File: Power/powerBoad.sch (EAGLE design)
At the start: 22 parts, among them CON1 MR30PW-M, CON2 XT30PW-M, U1 V7805-1000, U2 LD1117S33CTR, X1 JST-XH-06-PIN-LONG-PAD, X2 JST-XH-06-PIN-LONG-PAD, X3 JST-XH-06-PIN-LONG-PAD, X4 JST-XH-06-PIN-LONG-PAD

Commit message: 回路図と部品配置を検討し始めた
これからも検討に検討を重ね検討したいと思う。
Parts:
- removed U$7: XT30UPB-M, XT30UPB-M:XT30UPB-M
- added CON3: XT30PW-M, amass:XT30PW-M
- added J1: (no value), SparkFun-Connectors:CONN_05JST
- added KICK: (no value), jst-xh:S4B-XH-A
- added MC1, MC33151: MC33151DR2G, MC33151DR2G:MC33151DR2G
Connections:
- new net KICK1: MC33151.LOGIC_I/P_A
- new net KICK2: MC1.LOGIC_I/P_A
- new net KICK_V: KICK.2, MC33151.DRIVE_O/P_A
- new net KICK_V2: KICK.3, MC1.DRIVE_O/P_A
- new net TR_IN: KICK.4
- net +15V: now also CON3.+, MC1.VCC, MC33151.VCC; no longer U$7.1
- net +5V: now also KICK.1
- net GND: now also CON3.-, MC1.GND, MC33151.GND; no longer U$7.2
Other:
- note added: "Kick"
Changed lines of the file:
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@@
 <part name="+3V1" library="supply1" library_urn="urn:adsk.eagle:library:371" deviceset="+3V3" device=""/>
 <part name="P+5" library="supply1" library_urn="urn:adsk.eagle:library:371" deviceset="+15V" device=""/>
-<part name="U$7" library="XT30UPB-M" deviceset="XT30UPB-M" device=""/>
 <part name="D1" library="SS14" deviceset="SS14" device=""/>
 <part name="C1" library="rcl" library_urn="urn:adsk.eagle:library:334" deviceset="C-EU" device="C1608" package3d_urn="urn:adsk.eagle:package:23621/2" value="0.1u"/>
@@
 <part name="X3" library="Rembrandt Electronics - JST XH Connectors v1-0" deviceset="JST-XH-06-PIN" device="-LONG-PAD"/>
 <part name="X4" library="Rembrandt Electronics - JST XH Connectors v1-0" deviceset="JST-XH-06-PIN" device="-LONG-PAD"/>
+<part name="MC33151" library="MC33151DR2G" deviceset="MC33151DR2G" device=""/>
+<part name="P+3" library="supply1" library_urn="urn:adsk.eagle:library:371" deviceset="+15V" device=""/>
+<part name="MC1" library="MC33151DR2G" deviceset="MC33151DR2G" device=""/>
+<part name="GND2" library="supply1" library_urn="urn:adsk.eagle:library:371" deviceset="GND" device=""/>
+<part name="P+10" library="supply1" library_urn="urn:adsk.eagle:library:371" deviceset="+5V" device=""/>
+<part name="KICK" library="jst-xh" deviceset="S4B-XH-A" device=""/>
+<part name="CON3" library="amass" deviceset="XT30" device="PW-M"/>
+<part name="J1" library="SparkFun-Connectors" library_urn="urn:adsk.eagle:library:513" deviceset="CONN_05" device="JST" package3d_urn="urn:adsk.eagle:package:38120/1"/>
 </parts>
 <sheets>
@@
 <text x="-38.1" y="17.78" size="3.81" layer="94">Power</text>
 <text x="43.18" y="-38.1" size="3.81" layer="94">Dribbler</text>
+<text x="83.82" y="12.7" size="3.81" layer="94">Kick</text>
 </plain>
 <instances>
@@
 <attribute name="VALUE" x="58.42" y="-50.8" size="1.778" layer="96" rot="R90"/>
 </instance>
-<instance part="U$7" gate="G$1" x="-22.86" y="-38.1" smashed="yes"/>
 <instance part="D1" gate="G$1" x="-12.7" y="-71.12" smashed="yes" rot="R90">
 <attribute name="NAME" x="-15.24" y="-76.2" size="1.778" layer="95" rot="R90"/>
@@
 <instance part="X4" gate="-6" x="121.285" y="-82.55" smashed="yes">
 <attribute name="NAME" x="123.825" y="-83.312" size="1.524" layer="95"/>
+</instance>
+<instance part="MC33151" gate="G$1" x="91.44" y="2.54" smashed="yes">
+<attribute name="VALUE" x="90.17" y="7.62" size="1.778" layer="96" align="center-left"/>
+</instance>
+<instance part="P+3" gate="1" x="139.7" y="15.24" smashed="yes">
+<attribute name="VALUE" x="137.16" y="10.16" size="1.778" layer="96" rot="R90"/>
+</instance>
+<instance part="MC1" gate="G$1" x="91.44" y="-15.24" smashed="yes">
+<attribute name="VALUE" x="90.17" y="-10.16" size="1.778" layer="96" align="center-left"/>
+</instance>
+<instance part="GND2" gate="1" x="88.9" y="-33.02" smashed="yes">
+<attribute name="VALUE" x="86.36" y="-35.56" size="1.778" layer="96"/>
+</instance>
+<instance part="P+10" gate="1" x="88.9" y="38.1" smashed="yes">
+<attribute name="VALUE" x="86.36" y="33.02" size="1.778" layer="96" rot="R90"/>
+</instance>
+<instance part="KICK" gate="G$1" x="106.68" y="27.94" smashed="yes">
+<attribute name="NAME" x="102.87" y="34.29" size="1.778" layer="95"/>
+<attribute name="VALUE" x="102.87" y="17.78" size="1.778" layer="96"/>
+</instance>
+<instance part="CON3" gate="G$1" x="33.02" y="-40.64" smashed="yes">
+<attribute name="VALUE" x="29.21" y="-49.53" size="1.778" layer="96"/>
+<attribute name="NAME" x="29.21" y="-33.528" size="1.778" layer="95"/>
+</instance>
+<instance part="J1" gate="G$1" x="43.18" y="17.78" smashed="yes">
+<attribute name="VALUE" x="40.64" y="7.874" size="1.778" layer="96" font="vector"/>
+<attribute name="NAME" x="40.64" y="25.908" size="1.778" layer="95" font="vector"/>
 </instance>
 </instances>
@@
 <wire x1="-33.02" y1="-40.64" x2="-33.02" y2="-50.8" width="0.1524" layer="91"/>
 <pinref part="GND16" gate="1" pin="GND"/>
-<wire x1="-15.24" y1="-40.64" x2="-27.94" y2="-40.64" width="0.1524" layer="91"/>
+<wire x1="-15.24" y1="-40.64" x2="-33.02" y2="-40.64" width="0.1524" layer="91"/>
 <pinref part="U$2" gate="G$1" pin="2"/>
-<wire x1="-27.94" y1="-40.64" x2="-33.02" y2="-40.64" width="0.1524" layer="91"/>
-<pinref part="U$7" gate="G$1" pin="2"/>
-<junction x="-27.94" y="-40.64"/>
 <pinref part="CON2" gate="G$1" pin="-"/>
 <wire x1="22.86" y1="-43.18" x2="22.86" y2="-40.64" width="0.1524" layer="91"/>
 <wire x1="22.86" y1="-40.64" x2="-15.24" y2="-40.64" width="0.1524" layer="91"/>
 <junction x="-15.24" y="-40.64"/>
+<pinref part="CON3" gate="G$1" pin="-"/>
+<wire x1="38.1" y1="-43.18" x2="38.1" y2="-40.64" width="0.1524" layer="91"/>
+<wire x1="38.1" y1="-40.64" x2="22.86" y2="-40.64" width="0.1524" layer="91"/>
+<junction x="22.86" y="-40.64"/>
 </segment>
 <segment>
@@
 <pinref part="X4" gate="-3" pin="S"/>
 </segment>
+<segment>
+<pinref part="GND2" gate="1" pin="GND"/>
+<wire x1="88.9" y1="-20.32" x2="88.9" y2="-30.48" width="0.1524" layer="91"/>
+<pinref part="MC1" gate="G$1" pin="GND"/>
+<wire x1="91.44" y1="-20.32" x2="88.9" y2="-20.32" width="0.1524" layer="91"/>
+<pinref part="MC33151" gate="G$1" pin="GND"/>
+<wire x1="91.44" y1="-2.54" x2="88.9" y2="-2.54" width="0.1524" layer="91"/>
+<wire x1="88.9" y1="-2.54" x2="88.9" y2="-20.32" width="0.1524" layer="91"/>
+<junction x="88.9" y="-20.32"/>
+</segment>
 </net>
 <net name="+5V" class="0">
@@
 <junction x="12.7" y="-2.54"/>
 </segment>
+<segment>
+<wire x1="88.9" y1="30.48" x2="106.68" y2="30.48" width="0.1524" layer="91"/>
+<pinref part="P+10" gate="1" pin="+5V"/>
+<wire x1="88.9" y1="30.48" x2="88.9" y2="35.56" width="0.1524" layer="91"/>
+<pinref part="KICK" gate="G$1" pin="1"/>
+</segment>
 </net>
 <net name="+3V3" class="0">
@@
 <segment>
 <wire x1="-33.02" y1="-38.1" x2="-33.02" y2="-30.48" width="0.1524" layer="91"/>
-<wire x1="-15.24" y1="-38.1" x2="-27.94" y2="-38.1" width="0.1524" layer="91"/>
+<wire x1="-15.24" y1="-38.1" x2="-33.02" y2="-38.1" width="0.1524" layer="91"/>
 <pinref part="P+13" gate="1" pin="+15V"/>
 <pinref part="U$2" gate="G$1" pin="1"/>
-<wire x1="-27.94" y1="-38.1" x2="-33.02" y2="-38.1" width="0.1524" layer="91"/>
 <junction x="-15.24" y="-38.1"/>
-<pinref part="U$7" gate="G$1" pin="1"/>
-<junction x="-27.94" y="-38.1"/>
 <pinref part="CON2" gate="G$1" pin="+"/>
 <wire x1="-15.24" y1="-38.1" x2="22.86" y2="-38.1" width="0.1524" layer="91"/>
+<pinref part="CON3" gate="G$1" pin="+"/>
+<wire x1="38.1" y1="-38.1" x2="22.86" y2="-38.1" width="0.1524" layer="91"/>
+<junction x="22.86" y="-38.1"/>
 </segment>
 <segment>
@@
 <pinref part="CON1" gate="G$1" pin="2"/>
 <wire x1="55.88" y1="-63.5" x2="60.96" y2="-63.5" width="0.1524" layer="91"/>
+</segment>
+<segment>
+<pinref part="MC33151" gate="G$1" pin="VCC"/>
+<wire x1="137.16" y1="-2.54" x2="139.7" y2="-2.54" width="0.1524" layer="91"/>
+<wire x1="139.7" y1="-2.54" x2="139.7" y2="12.7" width="0.1524" layer="91"/>
+<pinref part="P+3" gate="1" pin="+15V"/>
+<pinref part="MC1" gate="G$1" pin="VCC"/>
+<wire x1="137.16" y1="-20.32" x2="139.7" y2="-20.32" width="0.1524" layer="91"/>
+<wire x1="139.7" y1="-20.32" x2="139.7" y2="-2.54" width="0.1524" layer="91"/>
+<junction x="139.7" y="-2.54"/>
 </segment>
 </net>
@@
 </segment>
 </net>
+<net name="KICK2" class="0">
+<segment>
+<pinref part="MC1" gate="G$1" pin="LOGIC_I/P_A"/>
+<wire x1="91.44" y1="-17.78" x2="86.36" y2="-17.78" width="0.1524" layer="91"/>
+<label x="86.36" y="-17.78" size="0.762" layer="95" rot="R180" xref="yes"/>
+</segment>
+</net>
+<net name="KICK_V2" class="0">
+<segment>
+<pinref part="MC1" gate="G$1" pin="DRIVE_O/P_A"/>
+<wire x1="137.16" y1="-17.78" x2="142.24" y2="-17.78" width="0.1524" layer="91"/>
+<label x="142.24" y="-17.78" size="0.762" layer="95" xref="yes"/>
+</segment>
+<segment>
+<wire x1="106.68" y1="25.4" x2="91.44" y2="25.4" width="0.1524" layer="91"/>
+<pinref part="KICK" gate="G$1" pin="3"/>
+<label x="91.44" y="25.4" size="0.762" layer="95" rot="R180" xref="yes"/>
+</segment>
+</net>
+<net name="KICK_V" class="0">
+<segment>
+<pinref part="MC33151" gate="G$1" pin="DRIVE_O/P_A"/>
+<wire x1="137.16" y1="0" x2="142.24" y2="0" width="0.1524" layer="91"/>
+<label x="142.24" y="0" size="0.762" layer="95" xref="yes"/>
+</segment>
+<segment>
+<wire x1="106.68" y1="27.94" x2="91.44" y2="27.94" width="0.1524" layer="91"/>
+<pinref part="KICK" gate="G$1" pin="2"/>
+<label x="91.44" y="27.94" size="0.762" layer="95" rot="R180" xref="yes"/>
+</segment>
+</net>
+<net name="KICK1" class="0">
+<segment>
+<pinref part="MC33151" gate="G$1" pin="LOGIC_I/P_A"/>
+<wire x1="91.44" y1="0" x2="86.36" y2="0" width="0.1524" layer="91"/>
+<label x="86.36" y="0" size="0.762" layer="95" rot="R180" xref="yes"/>
+</segment>
+</net>
+<net name="TR_IN" class="0">
+<segment>
+<wire x1="106.68" y1="22.86" x2="91.44" y2="22.86" width="0.1524" layer="91"/>
+<pinref part="KICK" gate="G$1" pin="4"/>
+<label x="91.44" y="22.86" size="0.762" layer="95" rot="R180" xref="yes"/>
+</segment>
+</net>

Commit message: some update 部品配置
# ==== Emojis ====
# ✨ :sparkles: Add new feature
# ✅  :white_check_mark: Update existing feature (not bug)
# ⚠️  :warning: Fix bug/error
# 🔥  :fire: Remove files or features
# ✏️ :pencil2: Fix typos
# 📝  :memo: Update documentation
# ♻️  :recycle: Dependencies update
# 🐧  :penguin: Improved the Linux
# 🍎  :apple: Improved the macOS
# 🔖 :bookmark: Add new library
# 🎉  :tada: Initial commit

# ==== Format ====
# :emoji: Subject
#
# Commit body...

# ==== Messages ====
# 新規(ファイル)機能追加: Add
# 機能修正、既存機能追加（バグではない): Update
# リファクタリング: Clean
# ファイル名変更:
# 削除など: Remove
# バグ修正: Fix
# バージョンアップ: Upgrade
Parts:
- removed J1: (no value), SparkFun-Connectors:CONN_05JST
- removed U$2: XT30UPB-M, XT30UPB-M:XT30UPB-M
- removed X1, X2, X3, X4: JST-XH-06-PIN-LONG-PAD, Rembrandt Electronics - JST XH Connectors v1-0:JST-XH-06-PIN-LONG-PAD
- added CN1, CN2, CN3, CN4: (no value), jst-xh:S6B-XH-A
- added JP1, JP2: (no value), adafruit:PINHD-1X6
- renumbered MC1 to U4, MC33151 to U3
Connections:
- removed net DR_PWM: CON1.1
- removed net TR_IN: KICK.4
- removed net VOLT_SIG: D1.K
- new net BAT: D1.K, JP1.1
- new net DRIB_PWM: CON1.1, JP1.4
- new net GPIO0: JP1.6
- new net PHOTO: JP1.5, KICK.4
- net +15V: now also JP2.1; no longer U$2.1
- net +3V3: now also JP2.3
- net +5V: now also JP2.2
- net 5V: now also CN1.3, CN2.3, CN3.3, CN4.3; no longer X1-4.S, X2-4.S, X3-4.S, X4-4.S
- net CANH: now also CN1.2, CN2.2, CN3.2, CN4.2, JP1.2; no longer X1-5.S, X2-5.S, X3-5.S, X4-5.S
- net CANL: now also CN1.1, CN2.1, CN3.1, CN4.1, JP1.3; no longer X1-6.S, X2-6.S, X3-6.S, X4-6.S
- net GND: now also CN1.4, CN2.4, CN3.4, CN4.4, JP2.4; no longer U$2.2, X1-3.S, X2-3.S, X3-3.S, X4-3.S
- net GVDD_IN: now also CN1.6, CN2.6, CN3.6, CN4.6; no longer X1-1.S, X2-1.S, X3-1.S, X4-1.S
- net KICK1: now also JP2.5
- net KICK2: now also JP2.6
- net PVDD: now also CN1.5, CN2.5, CN3.5, CN4.5; no longer X1-2.S, X2-2.S, X3-2.S, X4-2.S
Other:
- note added: "battery"

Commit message: POWERをいい感じにした
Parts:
- removed R5: 100k, rcl:R-EU_0207/10
- removed R6: 470k, rcl:R-EU_0207/10
- added LED3: (no value), led:LEDCHIPLED_0603
- added R2: 470k, rcl:R-EU_R0603
- added R3: 100k, rcl:R-EU_R0603
- added R4: 5k, rcl:R-EU_R0603
- LED1: device led:LEDCHIP-LED0805 -> led:LEDCHIPLED_0603
- R1: value (none) -> 1k
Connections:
- net GVDD_IN renamed GVDD
- removed net +15V: C3.1, C8.+, CON1.2, CON2.+, CON3.+, JP2.1, R6.1, U1.+VIN, U3.VCC, U4.VCC
- removed net 5V: CN1.3, CN2.3, CN3.3, CN4.3
- removed net LED: R1.2
- new net N$1: LED3.A, R4.1
- net +3V3: now also R1.2
- net +5V: now also CN1.3, CN2.3, CN3.3, CN4.3, R4.2
- net 2: now also R2.2, R3.2; no longer R5.2, R6.2
- net GND: now also LED3.C, R3.1; no longer R5.1
- net PVDD: now also C3.1, C8.+, CON1.2, CON2.+, CON3.+, JP2.1, R2.1, U1.+VIN, U3.VCC, U4.VCC
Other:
- moved on the sheet: LED1

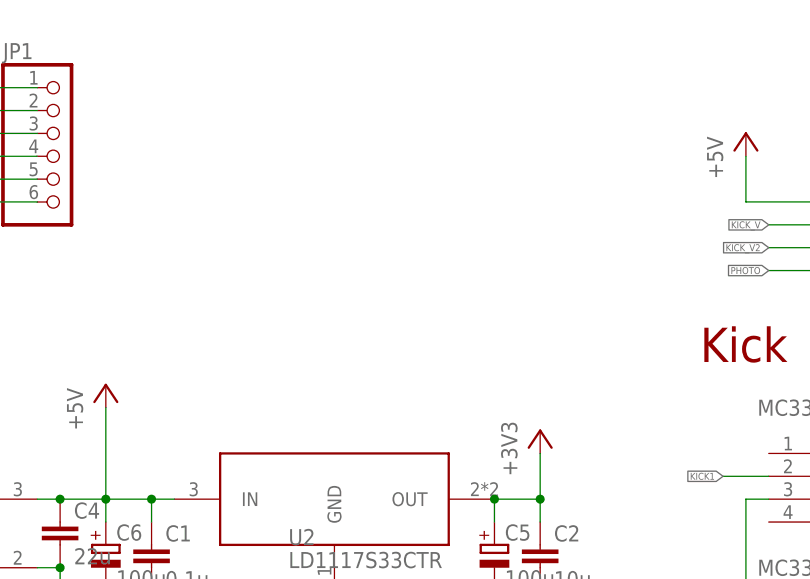
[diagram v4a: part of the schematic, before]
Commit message: 可変レギュレータを追加して配線をやりきった
次はパワみ化させる
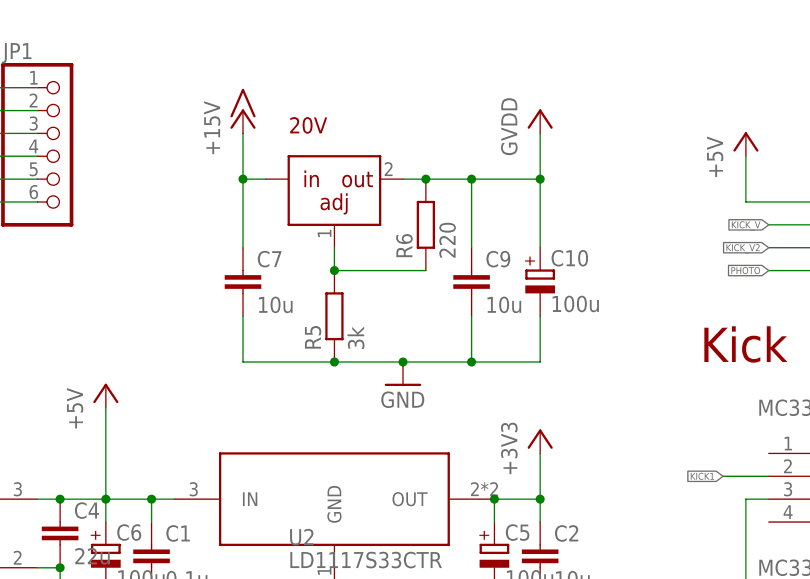
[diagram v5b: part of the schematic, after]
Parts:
- added C10: 100u, rcl:CPOL-EU153CLV-0605
- added C7, C9: 10u, rcl:C-EUC1608
- added R5: 3k, rcl:R-EU_R0603
- added R6: 220, rcl:R-EU_R0603
- added U$1: NJM317DL1, NJM317DL1:NJM317DL1
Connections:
- new net +15V: C7.1, U$1.IN
- new net N$5: R5.2, R6.1, U$1.ADJ
- net GND: now also C10.-, C7.2, C9.2, R5.1
- net GVDD: now also C10.+, C9.1, R6.2, U$1.OUT
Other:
- note added: "20V"
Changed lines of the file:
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@@
 <layer number="112" name="tSilk" color="7" fill="1" visible="no" active="no"/>
 <layer number="113" name="IDFDebug" color="7" fill="1" visible="no" active="no"/>
-<layer number="114" name="Badge_Outline" color="7" fill="1" visible="no" active="yes"/>
+<layer number="114" name="Badge_Outline" color="7" fill="1" visible="yes" active="yes"/>
 <layer number="115" name="ReferenceISLANDS" color="7" fill="1" visible="yes" active="yes"/>
 <layer number="116" name="Patch_BOT" color="9" fill="4" visible="no" active="no"/>
@@
 <part name="LED3" library="led" library_urn="urn:adsk.eagle:library:259" deviceset="LED" device="CHIPLED_0603" package3d_urn="urn:adsk.eagle:package:15822/2"/>
 <part name="LED1" library="led" library_urn="urn:adsk.eagle:library:259" deviceset="LED" device="CHIPLED_0603" package3d_urn="urn:adsk.eagle:package:15822/2"/>
+<part name="U$1" library="NJM317DL1" deviceset="NJM317DL1" device=""/>
+<part name="R5" library="rcl" library_urn="urn:adsk.eagle:library:334" deviceset="R-EU_" device="R0603" package3d_urn="urn:adsk.eagle:package:23555/3" value="3k"/>
+<part name="R6" library="rcl" library_urn="urn:adsk.eagle:library:334" deviceset="R-EU_" device="R0603" package3d_urn="urn:adsk.eagle:package:23555/3" value="220"/>
+<part name="C7" library="rcl" library_urn="urn:adsk.eagle:library:334" deviceset="C-EU" device="C1608" package3d_urn="urn:adsk.eagle:package:23621/2" value="10u"/>
+<part name="C9" library="rcl" library_urn="urn:adsk.eagle:library:334" deviceset="C-EU" device="C1608" package3d_urn="urn:adsk.eagle:package:23621/2" value="10u"/>
+<part name="C10" library="rcl" library_urn="urn:adsk.eagle:library:334" deviceset="CPOL-EU" device="153CLV-0605" package3d_urn="urn:adsk.eagle:package:23398/2" value="100u"/>
+<part name="P+6" library="supply1" library_urn="urn:adsk.eagle:library:371" deviceset="+15V" device=""/>
+<part name="GND1" library="supply1" library_urn="urn:adsk.eagle:library:371" deviceset="GND" device=""/>
+<part name="P+7" library="supply1" library_urn="urn:adsk.eagle:library:371" deviceset="+5V" device="" value="GVDD"/>
 </parts>
 <sheets>
@@
 <text x="83.82" y="12.7" size="3.81" layer="94">Kick</text>
 <text x="-40.64" y="43.18" size="0.762" layer="91" align="center">battery </text>
+<text x="38.1" y="38.1" size="1.778" layer="94">20V</text>
 </plain>
 <instances>
@@
 <attribute name="NAME" x="-34.544" y="-93.472" size="1.778" layer="95" rot="R90"/>
 <attribute name="VALUE" x="-32.385" y="-93.472" size="1.778" layer="96" rot="R90"/>
+</instance>
+<instance part="U$1" gate="G$1" x="43.18" y="33.02" smashed="yes"/>
+<instance part="R5" gate="G$1" x="43.18" y="17.78" smashed="yes" rot="R90">
+<attribute name="NAME" x="41.6814" y="13.97" size="1.778" layer="95" rot="R90"/>
+<attribute name="VALUE" x="46.482" y="13.97" size="1.778" layer="96" rot="R90"/>
+</instance>
+<instance part="R6" gate="G$1" x="53.34" y="27.94" smashed="yes" rot="R90">
+<attribute name="NAME" x="51.8414" y="24.13" size="1.778" layer="95" rot="R90"/>
+<attribute name="VALUE" x="56.642" y="24.13" size="1.778" layer="96" rot="R90"/>
+</instance>
+<instance part="C7" gate="G$1" x="33.02" y="22.86" smashed="yes">
+<attribute name="NAME" x="34.544" y="23.241" size="1.778" layer="95"/>
+<attribute name="VALUE" x="34.544" y="18.161" size="1.778" layer="96"/>
+</instance>
+<instance part="C9" gate="G$1" x="58.42" y="22.86" smashed="yes">
+<attribute name="NAME" x="59.944" y="23.241" size="1.778" layer="95"/>
+<attribute name="VALUE" x="59.944" y="18.161" size="1.778" layer="96"/>
+</instance>
+<instance part="C10" gate="G$1" x="66.04" y="22.86" smashed="yes">
+<attribute name="NAME" x="67.183" y="23.3426" size="1.778" layer="95"/>
+<attribute name="VALUE" x="67.183" y="18.2626" size="1.778" layer="96"/>
+</instance>
+<instance part="P+6" gate="1" x="33.02" y="40.64" smashed="yes">
+<attribute name="VALUE" x="30.48" y="35.56" size="1.778" layer="96" rot="R90"/>
+</instance>
+<instance part="GND1" gate="1" x="50.8" y="10.16" smashed="yes">
+<attribute name="VALUE" x="48.26" y="7.62" size="1.778" layer="96"/>
+</instance>
+<instance part="P+7" gate="1" x="66.04" y="40.64" smashed="yes">
+<attribute name="VALUE" x="63.5" y="35.56" size="1.778" layer="96" rot="R90"/>
 </instance>
 </instances>
@@
 <pinref part="JP2" gate="A" pin="4"/>
 </segment>
+<segment>
+<pinref part="R5" gate="G$1" pin="1"/>
+<wire x1="43.18" y1="12.7" x2="50.8" y2="12.7" width="0.1524" layer="91"/>
+<wire x1="50.8" y1="12.7" x2="58.42" y2="12.7" width="0.1524" layer="91"/>
+<wire x1="43.18" y1="12.7" x2="33.02" y2="12.7" width="0.1524" layer="91"/>
+<junction x="43.18" y="12.7"/>
+<pinref part="C7" gate="G$1" pin="2"/>
+<wire x1="33.02" y1="17.78" x2="33.02" y2="12.7" width="0.1524" layer="91"/>
+<pinref part="C9" gate="G$1" pin="2"/>
+<wire x1="58.42" y1="17.78" x2="58.42" y2="12.7" width="0.1524" layer="91"/>
+<junction x="58.42" y="12.7"/>
+<pinref part="C10" gate="G$1" pin="-"/>
+<wire x1="66.04" y1="17.78" x2="66.04" y2="12.7" width="0.1524" layer="91"/>
+<wire x1="66.04" y1="12.7" x2="58.42" y2="12.7" width="0.1524" layer="91"/>
+<pinref part="GND1" gate="1" pin="GND"/>
+<junction x="50.8" y="12.7"/>
+</segment>
 </net>
 <net name="+5V" class="1">
@@
 <pinref part="CN2" gate="G$1" pin="6"/>
 </segment>
-</net>
+<segment>
+<pinref part="U$1" gate="G$1" pin="OUT"/>
+<wire x1="50.8" y1="33.02" x2="53.34" y2="33.02" width="0.1524" layer="91"/>
+<pinref part="R6" gate="G$1" pin="2"/>
+<wire x1="53.34" y1="33.02" x2="58.42" y2="33.02" width="0.1524" layer="91"/>
+<junction x="53.34" y="33.02"/>
+<wire x1="58.42" y1="33.02" x2="58.42" y2="25.4" width="0.1524" layer="91"/>
+<wire x1="58.42" y1="33.02" x2="66.04" y2="33.02" width="0.1524" layer="91"/>
+<junction x="58.42" y="33.02"/>
+<pinref part="C9" gate="G$1" pin="1"/>
+<pinref part="C10" gate="G$1" pin="+"/>
+<wire x1="66.04" y1="33.02" x2="66.04" y2="25.4" width="0.1524" layer="91"/>
+<pinref part="P+7" gate="1" pin="+5V"/>
+<wire x1="66.04" y1="38.1" x2="66.04" y2="33.02" width="0.1524" layer="91"/>
+<junction x="66.04" y="33.02"/>
+</segment>
+</net>
+<net name="N$5" class="0">
+<segment>
+<pinref part="U$1" gate="G$1" pin="ADJ"/>
+<wire x1="43.18" y1="25.4" x2="43.18" y2="22.86" width="0.1524" layer="91"/>
+<pinref part="R5" gate="G$1" pin="2"/>
+<pinref part="R6" gate="G$1" pin="1"/>
+<wire x1="53.34" y1="22.86" x2="43.18" y2="22.86" width="0.1524" layer="91"/>
+<junction x="43.18" y="22.86"/>
+</segment>
+</net>
+<net name="+15V" class="0">
+<segment>
+<pinref part="U$1" gate="G$1" pin="IN"/>
+<wire x1="35.56" y1="33.02" x2="33.02" y2="33.02" width="0.1524" layer="91"/>
+<wire x1="33.02" y1="33.02" x2="33.02" y2="25.4" width="0.1524" layer="91"/>
+<junction x="33.02" y="33.02"/>
+<pinref part="C7" gate="G$1" pin="1"/>
+<pinref part="P+6" gate="1" pin="+15V"/>
+<wire x1="33.02" y1="38.1" x2="33.02" y2="33.02" width="0.1524" layer="91"/>
+</segment>
+</net>
